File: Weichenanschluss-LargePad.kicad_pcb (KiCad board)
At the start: 2 copper layers, 70.8 x 21.6 mm, 34 parts, among them J1 A1.1, J1001 Conn_01x01, J11 +V, J12 fb1, J13 fb2, J2 A1.2, J22 Za, J23 H, J25 g, J26 a, J27 Tg, J28 Ta, J29 GND, J3 Aux1, J30 GND, J31 +12, J32 Rü1, J33 Rü2, J4 Aux2, J41 g, J42 a, J43 +12V, J44 GND, J5 A2.1, J51 g, J52 a, J53 +12V, J54 GND, J6 A2.2, J7 Prz1, J8 Prz2, J9 -V

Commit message: Kicad 10
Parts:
- J21: renamed from J1001; value Conn_01x01 -> Zg

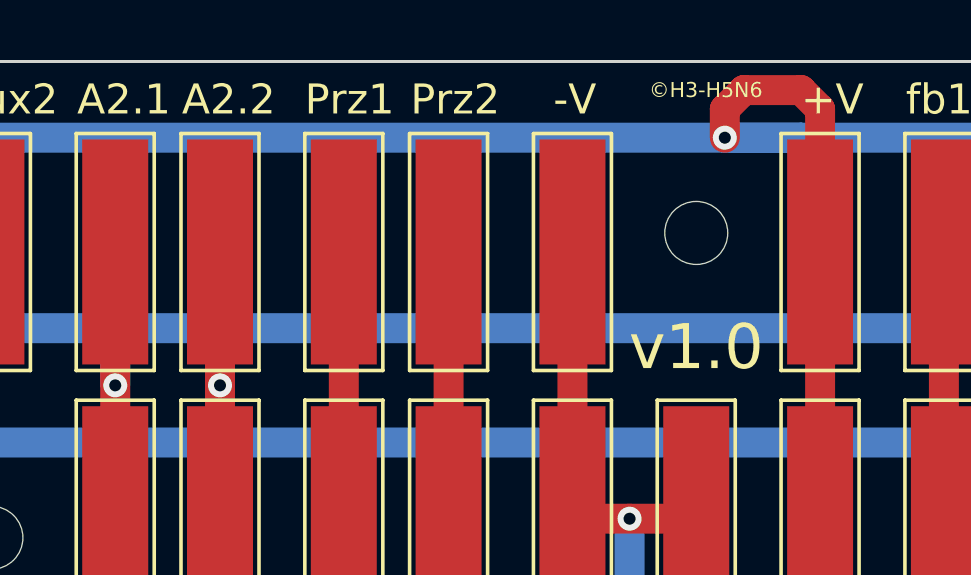
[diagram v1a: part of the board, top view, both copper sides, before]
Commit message: Name der Pad-Footprints angepasst: Wago->Connector_Misc
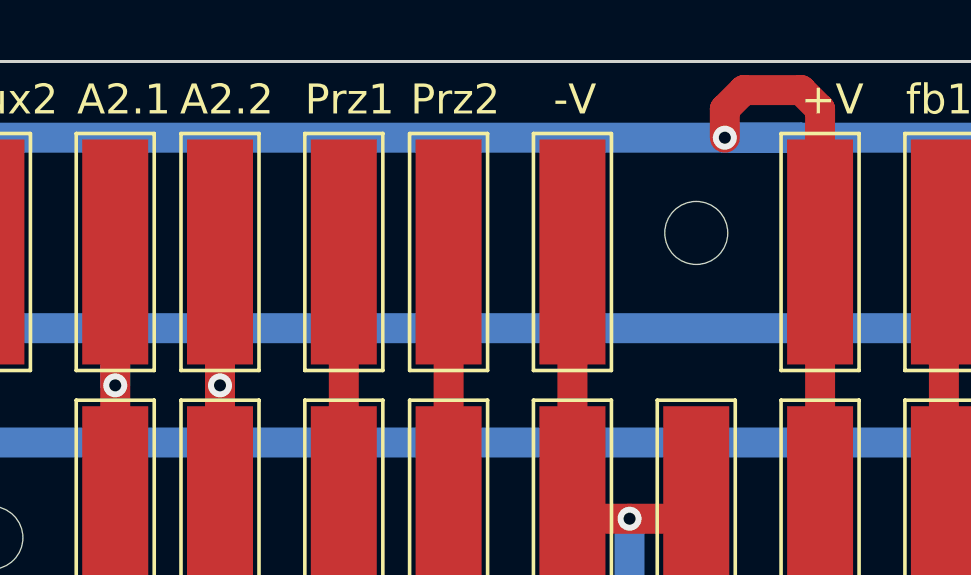
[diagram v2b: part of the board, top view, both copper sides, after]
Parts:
- added Tx1: ©H3-H5N6, Text:Text, F.Cu at (102.7, 79.9)
- added Tx2: Weichenanschluss-LargePad v1.1, Text:Text, F.Cu at (124.6, 89.5)
- J1, J11, J12, J13, J2, J21, J22, J23, J25, J26, J27, J28, J29, J3, J30, J31, J32, J33, J4, J41, J42, J43, J44, J5, J51, J52, J53, J54, J6, J7, J8, J9: footprint Wago:Pad_7.5x2.2mm -> Connector_Misc:Pad_7.5x2.2mm
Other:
- board text removed: "v1.0"
- board text removed: "©H3-H5N6"
- board text removed: "©H3-H5N6 2022 Weichenanschluss v1.0"
